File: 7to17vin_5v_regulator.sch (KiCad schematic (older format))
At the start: 13 parts

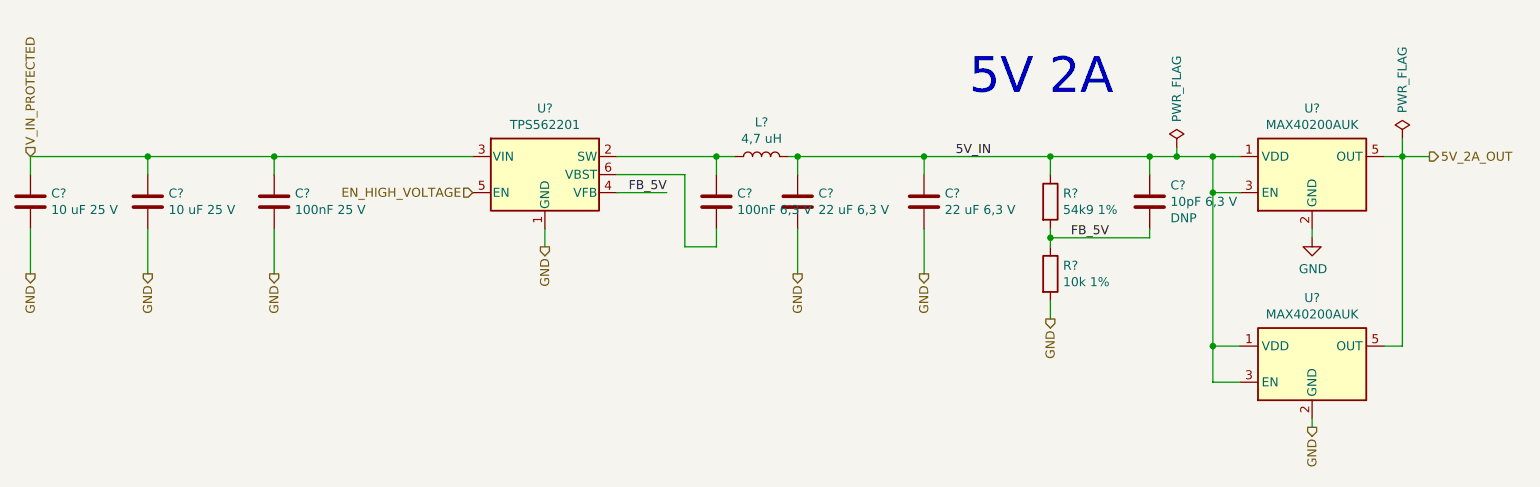
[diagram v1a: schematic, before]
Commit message: Schematic modified (Hierarchy) Bug where SPI was active when creset or ss was low fixed PCB layout started (almost all parts are at position) No parts on the bottom so far Arduino and PMOD header spacings corrected according to its standards
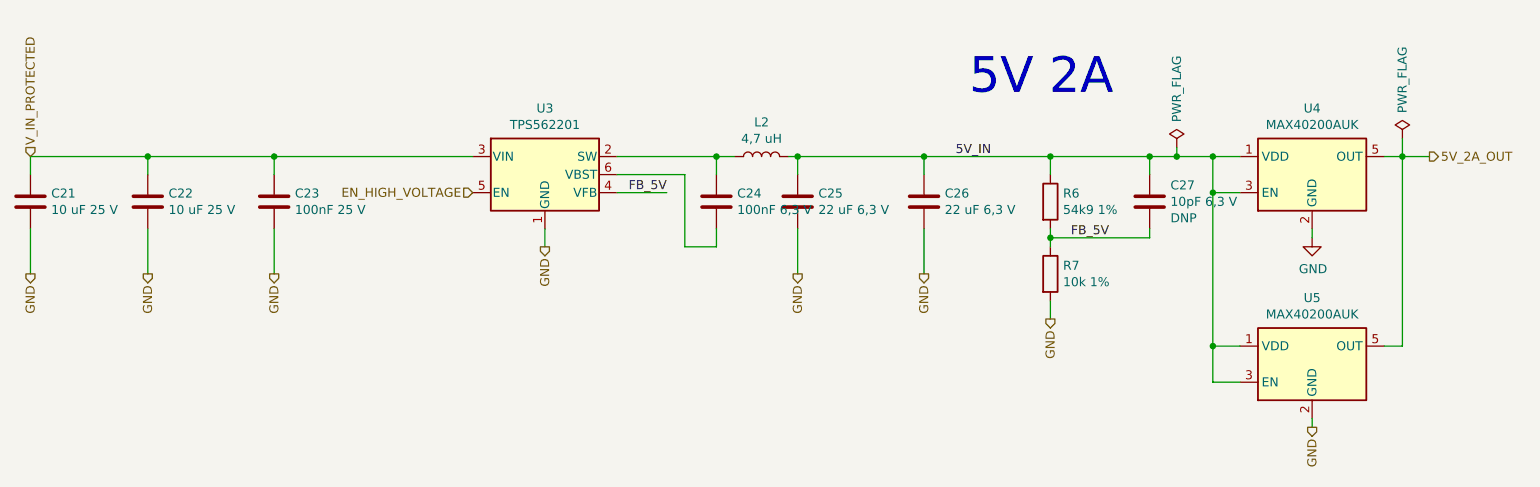
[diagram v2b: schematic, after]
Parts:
- gave numbers to parts that had none: 13
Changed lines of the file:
@@
 $Descr A4 11693 8268
 encoding utf-8
-Sheet 4 7
+Sheet 4 14
 Title ""
 Date ""
@@
 P 8050 2600
 AR Path="/5ECD2614/5F4C26A6" Ref="U?"  Part="1"
-AR Path="/5ECD2614/5F1EA733/5F4C26A6" Ref="U?"  Part="1"
-F 0 "U?" H 8050 2967 50  0000 C CNN
+AR Path="/5ECD2614/5F1EA733/5F4C26A6" Ref="U5"  Part="1"
+F 0 "U5" H 8050 2967 50  0000 C CNN
 F 1 "MAX40200AUK" H 8050 2876 50  0000 C CNN
 F 2 "Package_TO_SOT_SMD:SOT-23-5" H 8050 3100 50  0001 C CNN
@@
 P 8050 1900
 AR Path="/5ECD2614/5F4C26AC" Ref="#PWR?"  Part="1"
-AR Path="/5ECD2614/5F1EA733/5F4C26AC" Ref="#PWR?"  Part="1"
-F 0 "#PWR?" H 8050 1650 50  0001 C CNN
+AR Path="/5ECD2614/5F1EA733/5F4C26AC" Ref="#PWR025"  Part="1"
+F 0 "#PWR025" H 8050 1650 50  0001 C CNN
 F 1 "GND" H 8055 1727 50  0000 C CNN
 F 2 "" H 8050 1900 50  0001 C CNN
@@
 P 7300 1400
 AR Path="/5ECD2614/5F4C26B4" Ref="#FLG?"  Part="1"
-AR Path="/5ECD2614/5F1EA733/5F4C26B4" Ref="#FLG?"  Part="1"
-F 0 "#FLG?" H 7300 1475 50  0001 C CNN
+AR Path="/5ECD2614/5F1EA733/5F4C26B4" Ref="#FLG03"  Part="1"
+F 0 "#FLG03" H 7300 1475 50  0001 C CNN
 F 1 "PWR_FLAG" V 7300 1725 50  0000 C CNN
 F 2 "" H 7300 1400 50  0001 C CNN
@@
 P 8550 1350
 AR Path="/5ECD2614/5F4C26BE" Ref="#FLG?"  Part="1"
-AR Path="/5ECD2614/5F1EA733/5F4C26BE" Ref="#FLG?"  Part="1"
-F 0 "#FLG?" H 8550 1425 50  0001 C CNN
+AR Path="/5ECD2614/5F1EA733/5F4C26BE" Ref="#FLG04"  Part="1"
+F 0 "#FLG04" H 8550 1425 50  0001 C CNN
 F 1 "PWR_FLAG" V 8550 1675 50  0000 C CNN
 F 2 "" H 8550 1350 50  0001 C CNN
@@
 P 2300 1700
 AR Path="/5ECD2614/5F4C26DF" Ref="C?"  Part="1"
-AR Path="/5ECD2614/5F1EA733/5F4C26DF" Ref="C?"  Part="1"
-F 0 "C?" H 2415 1746 50  0000 L CNN
+AR Path="/5ECD2614/5F1EA733/5F4C26DF" Ref="C23"  Part="1"
+F 0 "C23" H 2415 1746 50  0000 L CNN
 F 1 "100nF 25 V" H 2415 1655 50  0000 L CNN
 F 2 "Capacitor_SMD:C_0603_1608Metric" H 2338 1550 50  0001 C CNN
@@
 P 950 1700
 AR Path="/5ECD2614/5F4C26ED" Ref="C?"  Part="1"
-AR Path="/5ECD2614/5F1EA733/5F4C26ED" Ref="C?"  Part="1"
-F 0 "C?" H 1065 1746 50  0000 L CNN
+AR Path="/5ECD2614/5F1EA733/5F4C26ED" Ref="C21"  Part="1"
+F 0 "C21" H 1065 1746 50  0000 L CNN
 F 1 "10 uF 25 V" H 1065 1655 50  0000 L CNN
 F 2 "Capacitor_SMD:C_0805_2012Metric" H 988 1550 50  0001 C CNN
@@
 P 1600 1700
 AR Path="/5ECD2614/5F4C26F8" Ref="C?"  Part="1"
-AR Path="/5ECD2614/5F1EA733/5F4C26F8" Ref="C?"  Part="1"
-F 0 "C?" H 1715 1746 50  0000 L CNN
+AR Path="/5ECD2614/5F1EA733/5F4C26F8" Ref="C22"  Part="1"
+F 0 "C22" H 1715 1746 50  0000 L CNN
 F 1 "10 uF 25 V" H 1715 1655 50  0000 L CNN
 F 2 "Capacitor_SMD:C_0805_2012Metric" H 1638 1550 50  0001 C CNN
@@
 P 4750 1700
 AR Path="/5ECD2614/5F4C270A" Ref="C?"  Part="1"
-AR Path="/5ECD2614/5F1EA733/5F4C270A" Ref="C?"  Part="1"
-F 0 "C?" H 4865 1746 50  0000 L CNN
+AR Path="/5ECD2614/5F1EA733/5F4C270A" Ref="C24"  Part="1"
+F 0 "C24" H 4865 1746 50  0000 L CNN
 F 1 "100nF 6,3 V" H 4865 1655 50  0000 L CNN
 F 2 "Capacitor_SMD:C_0603_1608Metric" H 4788 1550 50  0001 C CNN
@@
 P 8050 1550
 AR Path="/5ECD2614/5F4C272D" Ref="U?"  Part="1"
-AR Path="/5ECD2614/5F1EA733/5F4C272D" Ref="U?"  Part="1"
-F 0 "U?" H 8050 1917 50  0000 C CNN
+AR Path="/5ECD2614/5F1EA733/5F4C272D" Ref="U4"  Part="1"
+F 0 "U4" H 8050 1917 50  0000 C CNN
 F 1 "MAX40200AUK" H 8050 1826 50  0000 C CNN
 F 2 "Package_TO_SOT_SMD:SOT-23-5" H 8050 2050 50  0001 C CNN
@@
 P 7150 1700
 AR Path="/5ECD2614/5F4C2741" Ref="C?"  Part="1"
-AR Path="/5ECD2614/5F1EA733/5F4C2741" Ref="C?"  Part="1"
-F 0 "C?" H 7265 1791 50  0000 L CNN
+AR Path="/5ECD2614/5F1EA733/5F4C2741" Ref="C27"  Part="1"
+F 0 "C27" H 7265 1791 50  0000 L CNN
 F 1 "10pF 6,3 V" H 7265 1700 50  0000 L CNN
 F 2 "Capacitor_SMD:C_0603_1608Metric" H 7188 1550 50  0001 C CNN
@@
 P 6600 2100
 AR Path="/5ECD2614/5F4C2757" Ref="R?"  Part="1"
-AR Path="/5ECD2614/5F1EA733/5F4C2757" Ref="R?"  Part="1"
-F 0 "R?" H 6670 2146 50  0000 L CNN
+AR Path="/5ECD2614/5F1EA733/5F4C2757" Ref="R7"  Part="1"
+F 0 "R7" H 6670 2146 50  0000 L CNN
 F 1 "10k 1%" H 6670 2055 50  0000 L CNN
 F 2 "Resistor_SMD:R_0603_1608Metric" V 6530 2100 50  0001 C CNN
@@
 P 6600 1700
 AR Path="/5ECD2614/5F4C2762" Ref="R?"  Part="1"
-AR Path="/5ECD2614/5F1EA733/5F4C2762" Ref="R?"  Part="1"
-F 0 "R?" H 6670 1746 50  0000 L CNN
+AR Path="/5ECD2614/5F1EA733/5F4C2762" Ref="R6"  Part="1"
+F 0 "R6" H 6670 1746 50  0000 L CNN
 F 1 "54k9 1%" H 6670 1655 50  0000 L CNN
 F 2 "Resistor_SMD:R_0603_1608Metric" V 6530 1700 50  0001 C CNN
@@
 P 5000 1450
 AR Path="/5ECD2614/5F4C2781" Ref="L?"  Part="1"
-AR Path="/5ECD2614/5F1EA733/5F4C2781" Ref="L?"  Part="1"
-F 0 "L?" V 5190 1450 50  0000 C CNN
+AR Path="/5ECD2614/5F1EA733/5F4C2781" Ref="L2"  Part="1"
+F 0 "L2" V 5190 1450 50  0000 C CNN
 F 1 "4,7 uH" V 5099 1450 50  0000 C CNN
 F 2 "Inductor_SMD:L_Taiyo-Yuden_NR-50xx" H 5000 1450 50  0001 C CNN
@@
 P 5900 1700
 AR Path="/5ECD2614/5F4C278C" Ref="C?"  Part="1"
-AR Path="/5ECD2614/5F1EA733/5F4C278C" Ref="C?"  Part="1"
-F 0 "C?" H 6015 1746 50  0000 L CNN
+AR Path="/5ECD2614/5F1EA733/5F4C278C" Ref="C26"  Part="1"
+F 0 "C26" H 6015 1746 50  0000 L CNN
 F 1 "22 uF 6,3 V" H 6015 1655 50  0000 L CNN
 F 2 "Capacitor_SMD:C_0603_1608Metric" H 5938 1550 50  0001 C CNN
@@
 P 5200 1700
 AR Path="/5ECD2614/5F4C2797" Ref="C?"  Part="1"
-AR Path="/5ECD2614/5F1EA733/5F4C2797" Ref="C?"  Part="1"
-F 0 "C?" H 5315 1746 50  0000 L CNN
+AR Path="/5ECD2614/5F1EA733/5F4C2797" Ref="C25"  Part="1"
+F 0 "C25" H 5315 1746 50  0000 L CNN
 F 1 "22 uF 6,3 V" H 5315 1655 50  0000 L CNN
 F 2 "Capacitor_SMD:C_0603_1608Metric" H 5238 1550 50  0001 C CNN
@@
 P 3800 1550
 AR Path="/5ECD2614/5F4C27A2" Ref="U?"  Part="1"
-AR Path="/5ECD2614/5F1EA733/5F4C27A2" Ref="U?"  Part="1"
-F 0 "U?" H 3800 1917 50  0000 C CNN
+AR Path="/5ECD2614/5F1EA733/5F4C27A2" Ref="U3"  Part="1"
+F 0 "U3" H 3800 1917 50  0000 C CNN
 F 1 "TPS562201" H 3800 1826 50  0000 C CNN
 F 2 "Package_TO_SOT_SMD:SOT-23-6" H 3850 1300 50  0001 L CNN
